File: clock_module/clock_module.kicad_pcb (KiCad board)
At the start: 2 copper layers, 100 x 100 mm, 60 parts, among them J1 USB_C_Receptacle_PowerOnly_6P, J2 Conn_01x06_Socket, J3 Conn_01x08_Socket, SW1 SW_SPST, SW2 SW_Push, SW3 SW_SPDT, SW4 SW_SPDT, SW5 SW_DIP_x04, U1 74HC14, U10 74HC74, U11 74HC10, U2 74HC161N, U3 74HC161N, U4 74HC161N, U5 74HC161N, U6 74HC153, U7 74HC153, U8 74HC283, U9 74HC32

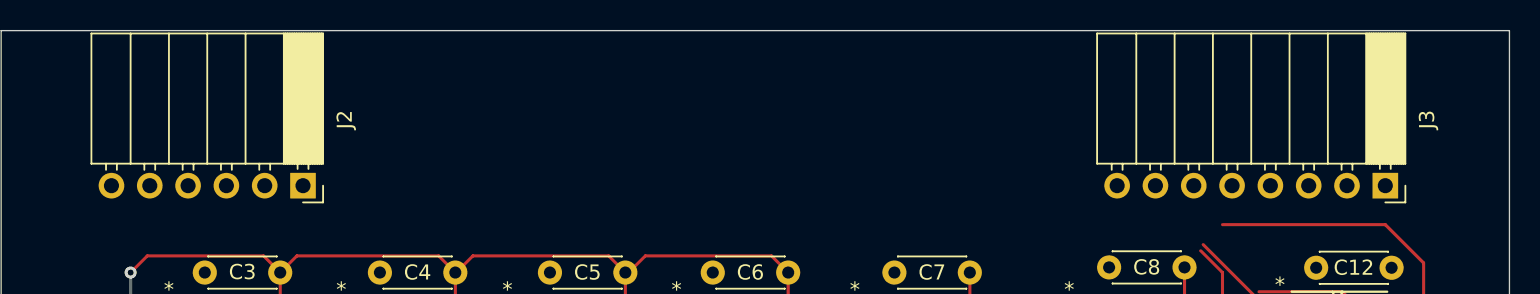
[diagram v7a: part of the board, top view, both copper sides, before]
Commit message: コネクタ位置調整
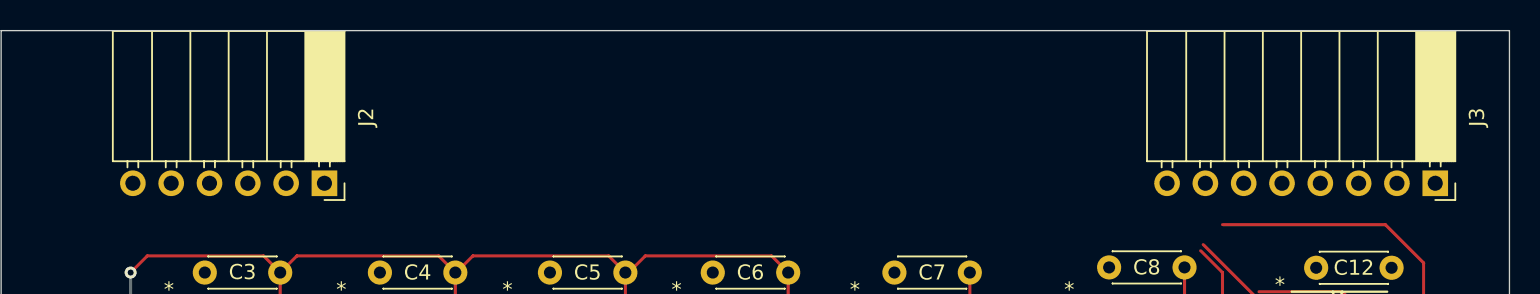
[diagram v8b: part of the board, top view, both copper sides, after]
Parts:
- moved J3 3.31 mm to (195.1, 60.1)
- moved J2 1.43 mm to (121.4, 60.1)
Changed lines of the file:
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@@
 	(footprint "Connector_PinSocket_2.54mm:PinSocket_1x08_P2.54mm_Horizontal"
 		(layer "F.Cu")
-		(at 191.77 60.28 -90)
+		(at 195.08 60.12 -90)
 		(descr "Through hole angled socket strip, 1x08, 2.54mm pitch, 8.51mm socket length, single row (from Kicad 4.0.7), script generated")
 		(tags "Through hole angled socket strip THT 1x08 2.54mm single row")
@@
 		)
 		(property "Value" "Conn_01x08_Socket"
-			(at -12.02 10.145 180)
+			(at -12.02 10.145 0)
 			(layer "F.Fab")
 			(effects
@@
 		)
 		(fp_text user "${REFERENCE}"
-			(at -5.775 8.89 360)
+			(at -5.775 8.89 0)
 			(layer "F.Fab")
 			(effects
@@
 		(tags "DIP Switch SPST Slide 7.62mm 300mil")
 		(property "Reference" "SW5"
-			(at -2.54 3.81 360)
+			(at -2.54 3.81 0)
 			(layer "F.SilkS")
 			(effects
@@
 		)
 		(fp_text user "${REFERENCE}"
-			(at 7.27 3.81 360)
+			(at 7.27 3.81 0)
 			(layer "F.Fab")
 			(effects
@@
 	(footprint "Connector_PinSocket_2.54mm:PinSocket_1x06_P2.54mm_Horizontal"
 		(layer "F.Cu")
-		(at 120.015 60.28 -90)
+		(at 121.435 60.12 -90)
 		(descr "Through hole angled socket strip, 1x06, 2.54mm pitch, 8.51mm socket length, single row (from Kicad 4.0.7), script generated")
 		(tags "Through hole angled socket strip THT 1x06 2.54mm single row")
@@
 		)
 		(property "Value" "Conn_01x06_Socket"
-			(at -12.02 6.325 180)
+			(at -12.02 6.325 360)
 			(layer "F.Fab")
 			(effects
@@
 		)
 		(fp_text user "${REFERENCE}"
-			(at -5.775 6.35 360)
+			(at -5.775 6.35 0)
 			(layer "F.Fab")
 			(effects
@@
 		(layer "Edge.Cuts")
 	)
+	(dimension
+		(type aligned)
+		(layer "User.1")
+		(pts
+			(xy 175.53 49.52) (xy 123.235 49.57)
+		)
+		(height 8.70958)
+		(gr_text "52.2950 mm"
+			(at 149.373073 39.685425 0.05478130037)
+			(layer "User.1")
+			(effects
+				(font
+					(size 1 1)
+					(thickness 0.15)
+				)
+			)
+		)
+		(format
+			(prefix "")
+			(suffix "")
+			(units 3)
+			(units_format 1)
+			(precision 4)
+		)
+		(style
+			(thickness 0.1)
+			(arrow_length 1.27)
+			(text_position_mode 0)
+			(extension_height 0.58642)
+			(extension_offset 0.5) keep_text_aligned)
+	)
 	(segment
